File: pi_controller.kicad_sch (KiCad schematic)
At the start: 123 parts, among them J1 PWM, J10 Conn_02x08_Counter_Clockwise, J11 Conn_02x08_Counter_Clockwise, J12 Conn_02x08_Counter_Clockwise, J13 Conn_02x08_Counter_Clockwise, J14 AN1, J15 AN2, J16 AN3, J17 AN4, J18 AN5, J19 AN6, J2 I2C, J20 AN7, J21 AN8, J22 AN9, J23 AN11, J24 AN13, J25 AN15, J26 AN10, J27 AN12, J28 AN14, J29 AN16, J3 SPI_LED, J4 SPI_DISPLAY, J5 9V, J6 Conn_02x08_Counter_Clockwise, J7 Conn_02x08_Counter_Clockwise, J8 Conn_02x08_Counter_Clockwise, J9 Conn_02x08_Counter_Clockwise, Q1 AOD4184A, U1 RaspberryPi_Pico, U2 PTMUX4051DYYR, U3 PTMUX4051DYYR, U4 PTMUX4051DYYR, U5 PTMUX4051DYYR, U6 74HC595, U7 74HC595

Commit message: Initial commit
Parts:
- removed D1, D10, D11, D12, D13, D14, D15, D16, D17, D18, D19, D2, D20, D21, D22, D23, D24, D25, D26, D27, D28, D29, D3, D30, D31, D32, D33, D34, D35, D36, D37, D38, D39, D4, D40, D41, D42, D43, D44, D45, D46, D47, D48, D49, D5, D50, D51, D52, D53, D54, D55, D56, D57, D58, D59, D6, D60, D61, D62, D63, D64, D7, D8, D9: 1N4148, symbol Device:D_Small
- removed J3: SPI_LED, Connector_PinHeader_1.00mm:PinHeader_2x04_P1.00mm_Vertical, symbol Connector_Generic:Conn_02x04_Odd_Even
- removed J4: SPI_DISPLAY, Connector_PinHeader_1.00mm:PinHeader_2x04_P1.00mm_Vertical, symbol Connector_Generic:Conn_02x04_Odd_Even
- removed J5: 9V, symbol Connector_Generic:Conn_01x02
- removed R5, R7: 13k, symbol Device:R_Small
- removed U2, U3, U4, U5: PTMUX4051DYYR, SOT-23-THIN16_DYY_TEX, symbol PTMUX4051:PTMUX4051DYYR
- removed U6, U7: 74HC595, symbol 74xx:74HC595
- added C10, C12, C8, C9: 0.1uF, Capacitor_SMD:C_0201_0603Metric_Pad0.64x0.40mm_HandSolder, symbol Device:C_Small
- added C11: 100uF, Capacitor_SMD:C_0201_0603Metric_Pad0.64x0.40mm_HandSolder, symbol Device:C_Small
- added C7: 2.2uF, Capacitor_SMD:C_0201_0603Metric_Pad0.64x0.40mm_HandSolder, symbol Device:C_Small
- added D1: LED, LED_SMD:LED_0805_2012Metric_Pad1.15x1.40mm_HandSolder, symbol Device:LED
- added D10, D11, D12, D13, D14, D15, D16, D17, D18, D19, D2, D20, D21, D22, D23, D24, D25, D26, D27, D28, D29, D3, D30, D31, D32, D33, D34, D35, D36, D37, D38, D39, D4, D40, D41, D42, D43, D44, D45, D46, D47, D48, D49, D5, D50, D51, D52, D53, D54, D55, D56, D57, D58, D59, D6, D60, D61, D62, D63, D64, D65, D7, D8, D9: BAT54J, Diode_SMD:D_SOD-323F, symbol Diode:BAT54J
- added J1: DC Supply, Connector_BarrelJack:BarrelJack_Horizontal, symbol Connector:Barrel_Jack_Switch
- added J10: SPI5, Connector_PinHeader_2.54mm:PinHeader_2x03_P2.54mm_Vertical, symbol Connector_Generic:Conn_02x03_Counter_Clockwise
- added J11: SPI7, Connector_PinHeader_2.54mm:PinHeader_2x03_P2.54mm_Vertical, symbol Connector_Generic:Conn_02x03_Counter_Clockwise
- added J15: LED1, Connector_PinHeader_2.54mm:PinHeader_2x08_P2.54mm_Vertical, symbol Connector_Generic:Conn_02x08_Counter_Clockwise
- added J16: LED2, Connector_PinHeader_2.54mm:PinHeader_2x08_P2.54mm_Vertical, symbol Connector_Generic:Conn_02x08_Counter_Clockwise
- added J17: LED3, Connector_PinHeader_2.54mm:PinHeader_2x08_P2.54mm_Vertical, symbol Connector_Generic:Conn_02x08_Counter_Clockwise
- added J18: LED4, Connector_PinHeader_2.54mm:PinHeader_2x08_P2.54mm_Vertical, symbol Connector_Generic:Conn_02x08_Counter_Clockwise
- added J22: LED5, Connector_PinHeader_2.54mm:PinHeader_2x08_P2.54mm_Vertical, symbol Connector_Generic:Conn_02x08_Counter_Clockwise
- added J23: LED6, Connector_PinHeader_2.54mm:PinHeader_2x08_P2.54mm_Vertical, symbol Connector_Generic:Conn_02x08_Counter_Clockwise
- added J24: LED7, Connector_PinHeader_2.54mm:PinHeader_2x08_P2.54mm_Vertical, symbol Connector_Generic:Conn_02x08_Counter_Clockwise
- added J25: LED8, Connector_PinHeader_2.54mm:PinHeader_2x08_P2.54mm_Vertical, symbol Connector_Generic:Conn_02x08_Counter_Clockwise
- added J3: UART, Connector_PinHeader_2.54mm:PinHeader_1x04_P2.54mm_Vertical, symbol Connector_Generic:Conn_01x04
- added J5: SPI2, Connector_PinHeader_2.54mm:PinHeader_2x03_P2.54mm_Vertical, symbol Connector_Generic:Conn_02x03_Counter_Clockwise
- added J6: SPI4, Connector_PinHeader_2.54mm:PinHeader_2x03_P2.54mm_Vertical, symbol Connector_Generic:Conn_02x03_Counter_Clockwise
- added J7: SPI6, Connector_PinHeader_2.54mm:PinHeader_2x03_P2.54mm_Vertical, symbol Connector_Generic:Conn_02x03_Counter_Clockwise
- added J8: SPI8, Connector_PinHeader_2.54mm:PinHeader_2x03_P2.54mm_Vertical, symbol Connector_Generic:Conn_02x03_Counter_Clockwise
- added J9: SPI3, Connector_PinHeader_2.54mm:PinHeader_2x03_P2.54mm_Vertical, symbol Connector_Generic:Conn_02x03_Counter_Clockwise
- added L1: 3.3uH, symbol Device:L
- added R11, R12: 3.3k, Resistor_SMD:R_0603_1608Metric_Pad0.98x0.95mm_HandSolder, symbol Device:R_Small
- added TP1, TP2, TP3, TP4: TestPoint, TestPoint:TestPoint_Pad_4.0x4.0mm, symbol Connector:TestPoint
- added U1: AP62300TWU, Package_TO_SOT_SMD:TSOT-23-6, symbol Regulator_Switching:AP62300TWU
- added U3: LM4040DBZ-3, Package_TO_SOT_SMD:SOT-23, symbol Reference_Voltage:LM4040DBZ-3
- added U4, U5: 74HC138, Package_SO:SOIC-16_3.9x9.9mm_P1.27mm, symbol 74xx:74HC138
- added U6: TM1639 (TA2009B), Package_SO:SOP-24_7.5x15.4mm_P1.27mm, symbol Titan_Micro:TM1639
- added U7: CD74HC4067SM96, Package_SO:SSOP-24_5.3x8.2mm_P0.65mm, symbol 74xx:CD74HC4067SM
- C1: value 0.1uF -> 10uF; footprint (none) -> Capacitor_SMD:C_1206_3216Metric_Pad1.33x1.80mm_HandSolder; JLCPCB Part # (none) -> C13585; Package (none) -> 1206; Temperature Rating (none) -> X5R; Tolerance (none) -> 10%; Voltage Rating (none) -> 50V
- C2: value 0.1uF -> 470nF; footprint (none) -> Capacitor_SMD:C_0603_1608Metric_Pad1.08x0.95mm_HandSolder; JLCPCB Part # (none) -> C1623; Package (none) -> 0603; Temperature Rating (none) -> X7R; Tolerance (none) -> 10%; Voltage Rating (none) -> 25V
- C3: value 0.1uF -> 220nF; footprint (none) -> Capacitor_SMD:C_0603_1608Metric_Pad1.08x0.95mm_HandSolder; JLCPCB Part # (none) -> C21120; Package (none) -> 0603; Tolerance (none) -> 10%; Voltage Rating (none) -> 25V
- C4: value 0.1uF -> 100pF; footprint (none) -> Capacitor_SMD:C_0201_0603Metric_Pad0.64x0.40mm_HandSolder; JLCPCB Part # (none) -> C14663; Package (none) -> 0603; Tolerance (none) -> 10%; Voltage Rating (none) -> 50V
- C5, C6: value 0.1uF -> 22uF; footprint (none) -> Capacitor_SMD:C_1206_3216Metric_Pad1.33x1.80mm_HandSolder; JLCPCB Part # (none) -> C12891; Package (none) -> 1206; Temperature Rating (none) -> X5R; Tolerance (none) -> 10%; Voltage Rating (none) -> 25V
- J12: renamed from J6; value Conn_02x08_Counter_Clockwise -> ROW1; footprint (none) -> Connector_PinHeader_2.54mm:PinHeader_2x08_P2.54mm_Vertical
- J13: renamed from J7; value Conn_02x08_Counter_Clockwise -> ROW2; footprint (none) -> Connector_PinHeader_2.54mm:PinHeader_2x08_P2.54mm_Vertical
- J14: renamed from J8; value Conn_02x08_Counter_Clockwise -> ROW3; footprint (none) -> Connector_PinHeader_2.54mm:PinHeader_2x08_P2.54mm_Vertical
- J19: renamed from J9; value Conn_02x08_Counter_Clockwise -> ROW4; footprint (none) -> Connector_PinHeader_2.54mm:PinHeader_2x08_P2.54mm_Vertical
- J2: footprint (none) -> Connector_PinHeader_2.54mm:PinHeader_1x04_P2.54mm_Vertical
- J20: renamed from J10; value Conn_02x08_Counter_Clockwise -> ROW5; footprint (none) -> Connector_PinHeader_2.54mm:PinHeader_2x08_P2.54mm_Vertical
- J21: renamed from J11; value Conn_02x08_Counter_Clockwise -> ROW6; footprint (none) -> Connector_PinHeader_2.54mm:PinHeader_2x08_P2.54mm_Vertical
- J26: renamed from J12; value Conn_02x08_Counter_Clockwise -> ROW7; footprint (none) -> Connector_PinHeader_2.54mm:PinHeader_2x08_P2.54mm_Vertical
- J27: renamed from J13; value Conn_02x08_Counter_Clockwise -> ROW8; footprint (none) -> Connector_PinHeader_2.54mm:PinHeader_2x08_P2.54mm_Vertical
- J28: renamed from J14; footprint (none) -> Connector_PinHeader_2.54mm:PinHeader_1x03_P2.54mm_Vertical
- J29: renamed from J16; footprint (none) -> Connector_PinHeader_2.54mm:PinHeader_1x03_P2.54mm_Vertical
- J30: renamed from J18; footprint (none) -> Connector_PinHeader_2.54mm:PinHeader_1x03_P2.54mm_Vertical
- J31: renamed from J20; footprint (none) -> Connector_PinHeader_2.54mm:PinHeader_1x03_P2.54mm_Vertical
- J32: renamed from J22; footprint (none) -> Connector_PinHeader_2.54mm:PinHeader_1x03_P2.54mm_Vertical
- J33: renamed from J23; footprint (none) -> Connector_PinHeader_2.54mm:PinHeader_1x03_P2.54mm_Vertical
- J34: renamed from J24; footprint (none) -> Connector_PinHeader_2.54mm:PinHeader_1x03_P2.54mm_Vertical
- J35: renamed from J25; footprint (none) -> Connector_PinHeader_2.54mm:PinHeader_1x03_P2.54mm_Vertical
- J36: renamed from J15; footprint (none) -> Connector_PinHeader_2.54mm:PinHeader_1x03_P2.54mm_Vertical
- J37: renamed from J17; footprint (none) -> Connector_PinHeader_2.54mm:PinHeader_1x03_P2.54mm_Vertical
- J38: renamed from J19; footprint (none) -> Connector_PinHeader_2.54mm:PinHeader_1x03_P2.54mm_Vertical
- J39: renamed from J21; footprint (none) -> Connector_PinHeader_2.54mm:PinHeader_1x03_P2.54mm_Vertical
- J4: renamed from J1; footprint (none) -> Connector_PinHeader_2.54mm:PinHeader_1x03_P2.54mm_Vertical
- J40: renamed from J26; footprint (none) -> Connector_PinHeader_2.54mm:PinHeader_1x03_P2.54mm_Vertical
- J41: renamed from J27; footprint (none) -> Connector_PinHeader_2.54mm:PinHeader_1x03_P2.54mm_Vertical
- J42: renamed from J28; footprint (none) -> Connector_PinHeader_2.54mm:PinHeader_1x03_P2.54mm_Vertical
- J43: renamed from J29; footprint (none) -> Connector_PinHeader_2.54mm:PinHeader_1x03_P2.54mm_Vertical
- Q1: footprint DPAK228P994X240-4N -> Package_TO_SOT_SMD:TO-252-2; JLCPCB Part # (none) -> C99124
- R1: renamed from R9; footprint (none) -> Resistor_SMD:R_0603_1608Metric_Pad0.98x0.95mm_HandSolder; JLCPCB Part # (none) -> C4190; Package (none) -> 0603; Power (none) -> 100mW; Tolerance (none) -> 1%
- R10: value 2.2k -> 3.3k; footprint (none) -> Resistor_SMD:R_0603_1608Metric_Pad0.98x0.95mm_HandSolder; JLCPCB Part # (none) -> C22978; Package (none) -> 0603; Power (none) -> 100mW; Tolerance (none) -> 1%
- R13, R14, R15, R16: value 10k -> 3.3k; footprint (none) -> Resistor_SMD:R_0603_1608Metric_Pad0.98x0.95mm_HandSolder; JLCPCB Part # (none) -> C22978; Package (none) -> 0603; Power (none) -> 100mW; Tolerance (none) -> 1%
- R2: value 13k -> 2.2k; footprint (none) -> Resistor_SMD:R_0603_1608Metric_Pad0.98x0.95mm_HandSolder; JLCPCB Part # (none) -> C4190; Package (none) -> 0603; Power (none) -> 100mW; Tolerance (none) -> 1%
- R3: value 13k -> 10k; footprint (none) -> Resistor_SMD:R_0603_1608Metric_Pad0.98x0.95mm_HandSolder; JLCPCB Part # (none) -> C25804; Package (none) -> 0603; Power (none) -> 100mW; Tolerance (none) -> 1%
- R4: value 13k -> 33.2k; footprint (none) -> Resistor_SMD:R_0603_1608Metric_Pad0.98x0.95mm_HandSolder; JLCPCB Part # (none) -> C23003; Package (none) -> 0603; Power (none) -> 100mW; Tolerance (none) -> 1%
- R5: renamed from R11; footprint (none) -> Resistor_SMD:R_0603_1608Metric_Pad0.98x0.95mm_HandSolder; JLCPCB Part # (none) -> C22775; Package (none) -> 0603; Power (none) -> 100mW; Tolerance (none) -> 1%
- R6: value 13k -> 330; footprint (none) -> Resistor_SMD:R_0603_1608Metric_Pad0.98x0.95mm_HandSolder; JLCPCB Part # (none) -> C23137; Package (none) -> 0603; Power (none) -> 100mW; Tolerance (none) -> 1%
- R7: renamed from R12; footprint (none) -> Resistor_SMD:R_0603_1608Metric_Pad0.98x0.95mm_HandSolder; JLCPCB Part # (none) -> C25804; Package (none) -> 0603; Power (none) -> 100mW; Tolerance (none) -> 1%
- R8: value 13k -> 47R; footprint (none) -> Resistor_SMD:R_0603_1608Metric_Pad0.98x0.95mm_HandSolder; JLCPCB Part # (none) -> C23182; Package (none) -> 0603; Power (none) -> 100mW; Tolerance (none) -> 1%
- R9: renamed from R1; value 13k -> 3.3k; footprint Resistor_SMD:R_0805_2012Metric -> Resistor_SMD:R_0603_1608Metric_Pad0.98x0.95mm_HandSolder; JLCPCB Part # (none) -> C22978; Package (none) -> 0603; Power (none) -> 100mW; Tolerance (none) -> 1%
- renumbered U1 to U2
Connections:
- net ADC0_MUX_CS is gone; now on net ROW6: U2.10 (GPIO7)
- net ADC1 is gone; now on net CS_LED: U2.32 (GPIO27_ADC1)
- net ROW_INPUT is gone; now on net ROW1: U2.1 (GPIO0)
- net ROW_MUX_A is gone; now on net ROW2: U2.2 (GPIO1)
- net ROW_MUX_B is gone; now on net ROW3: U2.4 (GPIO2)
- net ROW_MUX_C is gone; now on net ROW4: U2.5 (GPIO3)
- net ROW_MUX_CS is gone; now on net ROW5: U2.9 (GPIO6)
- net STEP_EN is gone; now on net ROW7: U2.19 (GPIO14)
- net STEP_RST is gone; now on net ROW8: U2.20 (GPIO15)
- net +3V3: now also C4.2, C5.2, C6.2, R10.1, R2.2, R4.2, R6.2, C10.1, C11.1, C12.1, C8.1, C9.1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; no longer C1.1, C2.1, C3.1, C4.1, C5.1, C6.1, J28.1 (Pin_1), J29.1 (Pin_1), J30.1 (Pin_1), J31.1 (Pin_1), J32.1 (Pin_1), J33.1 (Pin_1)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
- net +9V: now also C1.2, J1.1, U1.3 (IN)
- net ADC0: now also U7.1 (COM)
- net AN1: now also U7.9 (I0)
- net AN10: now also U7.22 (I9)
- net AN11: now also U7.21 (I10)
- net AN12: now also U7.20 (I11)
- net AN13: now also U7.19 (I12)
- net AN14: now also U7.18 (I13)
- net AN15: now also U7.17 (I14)
- net AN16: now also U7.16 (I15)
- net AN2: now also U7.8 (I1)
- net AN3: now also U7.7 (I2)
- net AN4: now also U7.6 (I3)
- net AN5: now also U7.5 (I4)
- net AN6: now also U7.4 (I5)
- net AN7: now also U7.3 (I6)
- net AN8: now also U7.2 (I7)
- net AN9: now also U7.23 (I8)
- net COL1: now also D2.1 (K), D26.1 (K), D27.1 (K), D28.1 (K), D3.1 (K), D4.1 (K), D50.1 (K), D51.1 (K), U4.15 (~{Y0})
- net COL2: now also D29.1 (K), D30.1 (K), D31.1 (K), D5.1 (K), D52.1 (K), D53.1 (K), D6.1 (K), D7.1 (K), U4.14 (~{Y1})
- net COL3: now also D10.1 (K), D32.1 (K), D33.1 (K), D34.1 (K), D54.1 (K), D55.1 (K), D8.1 (K), D9.1 (K), U4.13 (~{Y2})
- net COL4: now also D11.1 (K), D12.1 (K), D13.1 (K), D35.1 (K), D36.1 (K), D37.1 (K), D56.1 (K), D57.1 (K), U4.12 (~{Y3})
- net COL5: now also D14.1 (K), D15.1 (K), D16.1 (K), D38.1 (K), D39.1 (K), D40.1 (K), D58.1 (K), D59.1 (K), U4.11 (~{Y4})
- net COL6: now also D17.1 (K), D18.1 (K), D19.1 (K), D41.1 (K), D42.1 (K), D43.1 (K), D60.1 (K), D61.1 (K), U4.10 (~{Y5})
- net COL7: now also D20.1 (K), D21.1 (K), D22.1 (K), D44.1 (K), D45.1 (K), D46.1 (K), D62.1 (K), D63.1 (K), U4.9 (~{Y6})
- net COL8: now also D23.1 (K), D24.1 (K), D25.1 (K), D47.1 (K), D48.1 (K), D49.1 (K), D64.1 (K), D65.1 (K), U4.7 (~{Y7})
- net COL_MUX_A: now also U4.1 (A0), U5.1 (A0)
- net COL_MUX_B: now also U4.2 (A1), U5.2 (A1)
- net COL_MUX_C: now also U4.3 (A2), U5.3 (A2)
- net CS_LED: now also U5.6 (E2); no longer U2.22 (GPIO17)
- net GND: now also C1.1, C2.1, C5.1, C6.1, R3.1, C10.2, C11.2, C12.2, C7.2, C8.2, C9.2, D1.1 (K)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; no longer C1.2, C2.2, C3.2, C4.2, C5.2, C6.2
- net MISO: now also J10.5 (Pin_5), J11.5 (Pin_5), J5.5 (Pin_5), J6.5 (Pin_5), J7.5 (Pin_5), J8.5 (Pin_5), J9.5 (Pin_5)
- net MOSI: now also J10.1 (Pin_1), J11.1 (Pin_1), J5.1 (Pin_1), J6.1 (Pin_1), J7.1 (Pin_1), J8.1 (Pin_1), J9.1 (Pin_1), U6.6 (DIO)
- net ROW2: now also R10.2; no longer R2.2
- net ROW3: now also R11.2; no longer R3.2
- net ROW4: now also R12.2; no longer R4.2
- net ROW5: now also R13.2
- net ROW6: now also R14.2; no longer R6.2
- net ROW7: now also R15.2
- net ROW8: now also R16.2; no longer R8.2
- net +3.3VA renamed VDDA
- net ADC1_MUX_CS renamed ADC_MUX_B
- removed net CLR: R13.2, R16.2
- net COL_MUX_CS renamed ADC_MUX_D
- net CS_DISPLAY renamed ADC_MUX_A
- removed net OE_LED: R14.2, R15.2
- net STEP_CLK renamed UART0_RX
- net STEP_DIR renamed UART0_TX
- net STEP_SLEEP renamed ADC_MUX_C
- new net: C4.1, R3.2, R4.1, U1.4 (FB)
- new net: C3.1, U1.6 (BST)
- new net: C3.2, L1.1, U1.2 (SW)
- new net: C2.2, U1.5 (EN)
- new net: D1.2 (A), R6.1, TP2.1
- new net CS1: U5.15 (~{Y0}), U6.8 (~{STB})
- new net CS2: J5.3 (Pin_3), U5.14 (~{Y1})
- new net CS3: J9.3 (Pin_3), U5.13 (~{Y2})
- new net CS4: J6.3 (Pin_3), U5.12 (~{Y3})
- new net CS5: J10.3 (Pin_3), U5.11 (~{Y4})
- new net CS6: J7.3 (Pin_3), U5.10 (~{Y5})
- new net CS7: J11.3 (Pin_3), U5.9 (~{Y6})
- new net CS8: J8.3 (Pin_3), U5.7 (~{Y7})
- new net CS_KEY: U2.22 (GPIO17), U4.6 (E2)
- new net GRID1: J15.1 (Pin_1), J16.1 (Pin_1), J17.1 (Pin_1), J18.1 (Pin_1), J22.1 (Pin_1), J23.1 (Pin_1), J24.1 (Pin_1), J25.1 (Pin_1), U6.5 (GRID1)
- new net GRID2: J15.2 (Pin_2), J16.2 (Pin_2), J17.2 (Pin_2), J18.2 (Pin_2), J22.2 (Pin_2), J23.2 (Pin_2), J24.2 (Pin_2), J25.2 (Pin_2), U6.4 (GRID2)
- new net GRID3: J15.3 (Pin_3), J16.3 (Pin_3), J17.3 (Pin_3), J18.3 (Pin_3), J22.3 (Pin_3), J23.3 (Pin_3), J24.3 (Pin_3), J25.3 (Pin_3), U6.2 (GRID3)
- new net GRID4: J15.4 (Pin_4), J16.4 (Pin_4), J17.4 (Pin_4), J18.4 (Pin_4), J22.4 (Pin_4), J23.4 (Pin_4), J24.4 (Pin_4), J25.4 (Pin_4), U6.1 (GRID4)
- new net GRID5: J15.5 (Pin_5), J16.5 (Pin_5), J17.5 (Pin_5), J18.5 (Pin_5), J22.5 (Pin_5), J23.5 (Pin_5), J24.5 (Pin_5), J25.5 (Pin_5), U6.24 (GRID5)
- new net GRID6: J15.6 (Pin_6), J16.6 (Pin_6), J17.6 (Pin_6), J18.6 (Pin_6), J22.6 (Pin_6), J23.6 (Pin_6), J24.6 (Pin_6), J25.6 (Pin_6), U6.23 (GRID6)
- new net GRID7: J15.7 (Pin_7), J16.7 (Pin_7), J17.7 (Pin_7), J18.7 (Pin_7), J22.7 (Pin_7), J23.7 (Pin_7), J24.7 (Pin_7), J25.7 (Pin_7), U6.21 (GRID7)
- new net GRID8: J15.8 (Pin_8), J16.8 (Pin_8), J17.8 (Pin_8), J18.8 (Pin_8), J22.8 (Pin_8), J23.8 (Pin_8), J24.8 (Pin_8), J25.8 (Pin_8), U6.20 (GRID8)
- new net SEG1: J15.10 (Pin_10), J15.11 (Pin_11), J15.12 (Pin_12), J15.13 (Pin_13), J15.14 (Pin_14), J15.15 (Pin_15), J15.16 (Pin_16), J15.9 (Pin_9), U6.12 (SEG1/KS1)
- new net SEG10: J23.10 (Pin_10), J23.11 (Pin_11), J23.12 (Pin_12), J23.13 (Pin_13), J23.14 (Pin_14), J23.15 (Pin_15), J23.16 (Pin_16), J23.9 (Pin_9), U6.17 (SEG10)
- new net SEG11: J24.10 (Pin_10), J24.11 (Pin_11), J24.12 (Pin_12), J24.13 (Pin_13), J24.14 (Pin_14), J24.15 (Pin_15), J24.16 (Pin_16), J24.9 (Pin_9), U6.18 (SEG11)
- new net SEG12: J25.10 (Pin_10), J25.11 (Pin_11), J25.12 (Pin_12), J25.13 (Pin_13), J25.14 (Pin_14), J25.15 (Pin_15), J25.16 (Pin_16), J25.9 (Pin_9), U6.19 (SEG12)
- new net SEG2: J16.10 (Pin_10), J16.11 (Pin_11), J16.12 (Pin_12), J16.13 (Pin_13), J16.14 (Pin_14), J16.15 (Pin_15), J16.16 (Pin_16), J16.9 (Pin_9), U6.13 (SEG2/KS2)
- new net SEG3: J17.10 (Pin_10), J17.11 (Pin_11), J17.12 (Pin_12), J17.13 (Pin_13), J17.14 (Pin_14), J17.15 (Pin_15), J17.16 (Pin_16), J17.9 (Pin_9), U6.14 (SEG3/KS3)
- new net SEG4: J18.10 (Pin_10), J18.11 (Pin_11), J18.12 (Pin_12), J18.13 (Pin_13), J18.14 (Pin_14), J18.15 (Pin_15), J18.16 (Pin_16), J18.9 (Pin_9), U6.15 (SEG4/KS4)
- new net SEG9: J22.10 (Pin_10), J22.11 (Pin_11), J22.12 (Pin_12), J22.13 (Pin_13), J22.14 (Pin_14), J22.15 (Pin_15), J22.16 (Pin_16), J22.9 (Pin_9), U6.16 (SEG9)
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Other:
- note added: "I2C Output"
- note added: "Power Supply"
- note added: "UART Output"
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
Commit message: Update layout and rules
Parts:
- removed J10: SPI5, Connector_PinHeader_2.54mm:PinHeader_2x03_P2.54mm_Vertical, symbol Connector_Generic:Conn_02x03_Counter_Clockwise
- removed J11: SPI7, Connector_PinHeader_2.54mm:PinHeader_2x03_P2.54mm_Vertical, symbol Connector_Generic:Conn_02x03_Counter_Clockwise
- removed J12: ROW1, Connector_PinHeader_2.54mm:PinHeader_2x08_P2.54mm_Vertical, symbol Connector_Generic:Conn_02x08_Counter_Clockwise
- removed J13: ROW2, Connector_PinHeader_2.54mm:PinHeader_2x08_P2.54mm_Vertical, symbol Connector_Generic:Conn_02x08_Counter_Clockwise
- removed J14: ROW3, Connector_PinHeader_2.54mm:PinHeader_2x08_P2.54mm_Vertical, symbol Connector_Generic:Conn_02x08_Counter_Clockwise
- removed J15: LED1, Connector_PinHeader_2.54mm:PinHeader_2x08_P2.54mm_Vertical, symbol Connector_Generic:Conn_02x08_Counter_Clockwise
- removed J16: LED2, Connector_PinHeader_2.54mm:PinHeader_2x08_P2.54mm_Vertical, symbol Connector_Generic:Conn_02x08_Counter_Clockwise
- removed J17: LED3, Connector_PinHeader_2.54mm:PinHeader_2x08_P2.54mm_Vertical, symbol Connector_Generic:Conn_02x08_Counter_Clockwise
- removed J18: LED4, Connector_PinHeader_2.54mm:PinHeader_2x08_P2.54mm_Vertical, symbol Connector_Generic:Conn_02x08_Counter_Clockwise
- removed J19: ROW4, Connector_PinHeader_2.54mm:PinHeader_2x08_P2.54mm_Vertical, symbol Connector_Generic:Conn_02x08_Counter_Clockwise
- removed J20: ROW5, Connector_PinHeader_2.54mm:PinHeader_2x08_P2.54mm_Vertical, symbol Connector_Generic:Conn_02x08_Counter_Clockwise
- removed J21: ROW6, Connector_PinHeader_2.54mm:PinHeader_2x08_P2.54mm_Vertical, symbol Connector_Generic:Conn_02x08_Counter_Clockwise
- removed J22: LED5, Connector_PinHeader_2.54mm:PinHeader_2x08_P2.54mm_Vertical, symbol Connector_Generic:Conn_02x08_Counter_Clockwise
- removed J23: LED6, Connector_PinHeader_2.54mm:PinHeader_2x08_P2.54mm_Vertical, symbol Connector_Generic:Conn_02x08_Counter_Clockwise
- removed J24: LED7, Connector_PinHeader_2.54mm:PinHeader_2x08_P2.54mm_Vertical, symbol Connector_Generic:Conn_02x08_Counter_Clockwise
- removed J25: LED8, Connector_PinHeader_2.54mm:PinHeader_2x08_P2.54mm_Vertical, symbol Connector_Generic:Conn_02x08_Counter_Clockwise
- removed J26: ROW7, Connector_PinHeader_2.54mm:PinHeader_2x08_P2.54mm_Vertical, symbol Connector_Generic:Conn_02x08_Counter_Clockwise
- removed J27: ROW8, Connector_PinHeader_2.54mm:PinHeader_2x08_P2.54mm_Vertical, symbol Connector_Generic:Conn_02x08_Counter_Clockwise
- removed J5: SPI2, Connector_PinHeader_2.54mm:PinHeader_2x03_P2.54mm_Vertical, symbol Connector_Generic:Conn_02x03_Counter_Clockwise
- removed J6: SPI4, Connector_PinHeader_2.54mm:PinHeader_2x03_P2.54mm_Vertical, symbol Connector_Generic:Conn_02x03_Counter_Clockwise
- removed J7: SPI6, Connector_PinHeader_2.54mm:PinHeader_2x03_P2.54mm_Vertical, symbol Connector_Generic:Conn_02x03_Counter_Clockwise
- removed J8: SPI8, Connector_PinHeader_2.54mm:PinHeader_2x03_P2.54mm_Vertical, symbol Connector_Generic:Conn_02x03_Counter_Clockwise
- removed J9: SPI3, Connector_PinHeader_2.54mm:PinHeader_2x03_P2.54mm_Vertical, symbol Connector_Generic:Conn_02x03_Counter_Clockwise
- added J10: CS5, Connector_PinHeader_2.54mm:PinHeader_2x03_P2.54mm_Vertical, symbol Connector_Generic:Conn_02x03_Odd_Even
- added J11: CS7, Connector_PinHeader_2.54mm:PinHeader_2x03_P2.54mm_Vertical, symbol Connector_Generic:Conn_02x03_Odd_Even
- added J12: ROW1, Connector_PinHeader_2.54mm:PinHeader_2x08_P2.54mm_Vertical, symbol Connector_Generic:Conn_02x08_Odd_Even
- added J13: ROW2, Connector_PinHeader_2.54mm:PinHeader_2x08_P2.54mm_Vertical, symbol Connector_Generic:Conn_02x08_Odd_Even
- added J14: ROW3, Connector_PinHeader_2.54mm:PinHeader_2x08_P2.54mm_Vertical, symbol Connector_Generic:Conn_02x08_Odd_Even
- added J15: LED1, Connector_PinHeader_2.54mm:PinHeader_2x08_P2.54mm_Vertical, symbol Connector_Generic:Conn_02x08_Odd_Even
- added J16: LED2, Connector_PinHeader_2.54mm:PinHeader_2x08_P2.54mm_Vertical, symbol Connector_Generic:Conn_02x08_Odd_Even
- added J17: LED3, Connector_PinHeader_2.54mm:PinHeader_2x08_P2.54mm_Vertical, symbol Connector_Generic:Conn_02x08_Odd_Even
- added J18: LED4, Connector_PinHeader_2.54mm:PinHeader_2x08_P2.54mm_Vertical, symbol Connector_Generic:Conn_02x08_Odd_Even
- added J19: ROW4, Connector_PinHeader_2.54mm:PinHeader_2x08_P2.54mm_Vertical, symbol Connector_Generic:Conn_02x08_Odd_Even
- added J20: ROW5, Connector_PinHeader_2.54mm:PinHeader_2x08_P2.54mm_Vertical, symbol Connector_Generic:Conn_02x08_Odd_Even
- added J21: ROW6, Connector_PinHeader_2.54mm:PinHeader_2x08_P2.54mm_Vertical, symbol Connector_Generic:Conn_02x08_Odd_Even
- added J22: LED5, Connector_PinHeader_2.54mm:PinHeader_2x08_P2.54mm_Vertical, symbol Connector_Generic:Conn_02x08_Odd_Even
- added J23: LED6, Connector_PinHeader_2.54mm:PinHeader_2x08_P2.54mm_Vertical, symbol Connector_Generic:Conn_02x08_Odd_Even
- added J24: LED7, Connector_PinHeader_2.54mm:PinHeader_2x08_P2.54mm_Vertical, symbol Connector_Generic:Conn_02x08_Odd_Even
- added J25: LED8, Connector_PinHeader_2.54mm:PinHeader_2x08_P2.54mm_Vertical, symbol Connector_Generic:Conn_02x08_Odd_Even
- added J26: ROW7, Connector_PinHeader_2.54mm:PinHeader_2x08_P2.54mm_Vertical, symbol Connector_Generic:Conn_02x08_Odd_Even
- added J27: ROW8, Connector_PinHeader_2.54mm:PinHeader_2x08_P2.54mm_Vertical, symbol Connector_Generic:Conn_02x08_Odd_Even
- added J5: CS2, Connector_PinHeader_2.54mm:PinHeader_2x03_P2.54mm_Vertical, symbol Connector_Generic:Conn_02x03_Odd_Even
- added J6: CS4, Connector_PinHeader_2.54mm:PinHeader_2x03_P2.54mm_Vertical, symbol Connector_Generic:Conn_02x03_Odd_Even
- added J7: CS6, Connector_PinHeader_2.54mm:PinHeader_2x03_P2.54mm_Vertical, symbol Connector_Generic:Conn_02x03_Odd_Even
- added J8: CS8, Connector_PinHeader_2.54mm:PinHeader_2x03_P2.54mm_Vertical, symbol Connector_Generic:Conn_02x03_Odd_Even
- added J9: CS3, Connector_PinHeader_2.54mm:PinHeader_2x03_P2.54mm_Vertical, symbol Connector_Generic:Conn_02x03_Odd_Even
- L1: footprint (none) -> Inductor_SMD:L_Sunlord_MWSA0604S
- renumbered TP3 to TP1, TP1 to TP2, TP2 to TP3
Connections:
- net +3V3: now also J10.2 (Pin_2), J11.2 (Pin_2), J5.2 (Pin_2), J6.2 (Pin_2), J7.2 (Pin_2), J8.2 (Pin_2), J9.2 (Pin_2)
- net CS2: now also J5.5 (Pin_5)
- net CS3: now also J9.5 (Pin_5)
- net CS4: now also J6.5 (Pin_5)
- net CS5: now also J10.5 (Pin_5)
- net CS6: now also J7.5 (Pin_5)
- net CS7: now also J11.5 (Pin_5)
- net CS8: now also J8.5 (Pin_5)
- net GND: now also J10.6 (Pin_6), J11.6 (Pin_6), J5.6 (Pin_6), J6.6 (Pin_6), J7.6 (Pin_6), J8.6 (Pin_6), J9.6 (Pin_6)
- net GRID1: now also J15.16 (Pin_16), J16.16 (Pin_16), J17.16 (Pin_16), J18.16 (Pin_16), J22.16 (Pin_16), J23.16 (Pin_16), J24.16 (Pin_16), J25.16 (Pin_16)
- net GRID2: now also J15.14 (Pin_14), J16.14 (Pin_14), J17.14 (Pin_14), J18.14 (Pin_14), J22.14 (Pin_14), J23.14 (Pin_14), J24.14 (Pin_14), J25.14 (Pin_14)
- net GRID3: now also J15.12 (Pin_12), J16.12 (Pin_12), J17.12 (Pin_12), J18.12 (Pin_12), J22.12 (Pin_12), J23.12 (Pin_12), J24.12 (Pin_12), J25.12 (Pin_12)
- net GRID4: now also J15.10 (Pin_10), J16.10 (Pin_10), J17.10 (Pin_10), J18.10 (Pin_10), J22.10 (Pin_10), J23.10 (Pin_10), J24.10 (Pin_10), J25.10 (Pin_10)
- net GRID5: now also J15.8 (Pin_8), J16.8 (Pin_8), J17.8 (Pin_8), J18.8 (Pin_8), J22.8 (Pin_8), J23.8 (Pin_8), J24.8 (Pin_8), J25.8 (Pin_8)
- net GRID6: now also J15.6 (Pin_6), J16.6 (Pin_6), J17.6 (Pin_6), J18.6 (Pin_6), J22.6 (Pin_6), J23.6 (Pin_6), J24.6 (Pin_6), J25.6 (Pin_6)
- net GRID7: now also J15.4 (Pin_4), J16.4 (Pin_4), J17.4 (Pin_4), J18.4 (Pin_4), J22.4 (Pin_4), J23.4 (Pin_4), J24.4 (Pin_4), J25.4 (Pin_4)
- net GRID8: now also J15.2 (Pin_2), J16.2 (Pin_2), J17.2 (Pin_2), J18.2 (Pin_2), J22.2 (Pin_2), J23.2 (Pin_2), J24.2 (Pin_2), J25.2 (Pin_2)
- net MISO: now also J10.4 (Pin_4), J11.4 (Pin_4), J5.4 (Pin_4), J6.4 (Pin_4), J7.4 (Pin_4), J8.4 (Pin_4), J9.4 (Pin_4)
- net MOSI: now also J10.1 (Pin_1), J11.1 (Pin_1), J5.1 (Pin_1), J6.1 (Pin_1), J7.1 (Pin_1), J8.1 (Pin_1), J9.1 (Pin_1)
- net ROW1: now also J12.10 (Pin_10), J12.12 (Pin_12), J12.14 (Pin_14), J12.16 (Pin_16), J12.2 (Pin_2), J12.4 (Pin_4), J12.6 (Pin_6), J12.8 (Pin_8)
- net ROW2: now also J13.10 (Pin_10), J13.12 (Pin_12), J13.14 (Pin_14), J13.16 (Pin_16), J13.2 (Pin_2), J13.4 (Pin_4), J13.6 (Pin_6), J13.8 (Pin_8)
- net ROW3: now also J14.10 (Pin_10), J14.12 (Pin_12), J14.14 (Pin_14), J14.16 (Pin_16), J14.2 (Pin_2), J14.4 (Pin_4), J14.6 (Pin_6), J14.8 (Pin_8)
- net ROW4: now also J19.10 (Pin_10), J19.12 (Pin_12), J19.14 (Pin_14), J19.16 (Pin_16), J19.2 (Pin_2), J19.4 (Pin_4), J19.6 (Pin_6), J19.8 (Pin_8)
- net ROW5: now also J20.10 (Pin_10), J20.12 (Pin_12), J20.14 (Pin_14), J20.16 (Pin_16), J20.2 (Pin_2), J20.4 (Pin_4), J20.6 (Pin_6), J20.8 (Pin_8)
- net ROW6: now also J21.10 (Pin_10), J21.12 (Pin_12), J21.14 (Pin_14), J21.16 (Pin_16), J21.2 (Pin_2), J21.4 (Pin_4), J21.6 (Pin_6), J21.8 (Pin_8)
- net ROW7: now also J26.10 (Pin_10), J26.12 (Pin_12), J26.14 (Pin_14), J26.16 (Pin_16), J26.2 (Pin_2), J26.4 (Pin_4), J26.6 (Pin_6), J26.8 (Pin_8)
- net ROW8: now also J27.10 (Pin_10), J27.12 (Pin_12), J27.14 (Pin_14), J27.16 (Pin_16), J27.2 (Pin_2), J27.4 (Pin_4), J27.6 (Pin_6), J27.8 (Pin_8)
- net SCLK: now also J10.3 (Pin_3), J11.3 (Pin_3), J5.3 (Pin_3), J6.3 (Pin_3), J7.3 (Pin_3), J8.3 (Pin_3), J9.3 (Pin_3)
- net SEG1: now also J15.1 (Pin_1), J15.11 (Pin_11), J15.13 (Pin_13), J15.15 (Pin_15), J15.3 (Pin_3), J15.5 (Pin_5), J15.7 (Pin_7), J15.9 (Pin_9)
- net SEG10: now also J23.1 (Pin_1), J23.11 (Pin_11), J23.13 (Pin_13), J23.15 (Pin_15), J23.3 (Pin_3), J23.5 (Pin_5), J23.7 (Pin_7), J23.9 (Pin_9)
- net SEG11: now also J24.1 (Pin_1), J24.11 (Pin_11), J24.13 (Pin_13), J24.15 (Pin_15), J24.3 (Pin_3), J24.5 (Pin_5), J24.7 (Pin_7), J24.9 (Pin_9)
- net SEG12: now also J25.1 (Pin_1), J25.11 (Pin_11), J25.13 (Pin_13), J25.15 (Pin_15), J25.3 (Pin_3), J25.5 (Pin_5), J25.7 (Pin_7), J25.9 (Pin_9)
- net SEG2: now also J16.1 (Pin_1), J16.11 (Pin_11), J16.13 (Pin_13), J16.15 (Pin_15), J16.3 (Pin_3), J16.5 (Pin_5), J16.7 (Pin_7), J16.9 (Pin_9)
- net SEG3: now also J17.1 (Pin_1), J17.11 (Pin_11), J17.13 (Pin_13), J17.15 (Pin_15), J17.3 (Pin_3), J17.5 (Pin_5), J17.7 (Pin_7), J17.9 (Pin_9)
- net SEG4: now also J18.1 (Pin_1), J18.11 (Pin_11), J18.13 (Pin_13), J18.15 (Pin_15), J18.3 (Pin_3), J18.5 (Pin_5), J18.7 (Pin_7), J18.9 (Pin_9)
- net SEG9: now also J22.1 (Pin_1), J22.11 (Pin_11), J22.13 (Pin_13), J22.15 (Pin_15), J22.3 (Pin_3), J22.5 (Pin_5), J22.7 (Pin_7), J22.9 (Pin_9)
- net at D51.2 (A): now also J27.1 (Pin_1)
- net at D5.2 (A): now also J12.3 (Pin_3)
- net at D64.2 (A): now also J26.15 (Pin_15)
- net at D46.2 (A): now also J21.13 (Pin_13)
- net at D27.2 (A): now also J20.1 (Pin_1)
- net at D30.2 (A): now also J20.3 (Pin_3)
- net at D33.2 (A): now also J20.5 (Pin_5)
- net at D36.2 (A): now also J20.7 (Pin_7)
- net at D39.2 (A): now also J20.9 (Pin_9)
- net at D42.2 (A): now also J20.11 (Pin_11)
- net at D45.2 (A): now also J20.13 (Pin_13)
- net at D48.2 (A): now also J20.15 (Pin_15)
- net at D47.2 (A): now also J19.15 (Pin_15)
- net at D11.2 (A): now also J12.7 (Pin_7)
- net at D50.2 (A): now also J26.1 (Pin_1)
- net at D52.2 (A): now also J26.3 (Pin_3)
- net at D54.2 (A): now also J26.5 (Pin_5)
- net at D56.2 (A): now also J26.7 (Pin_7)
- net at D58.2 (A): now also J26.9 (Pin_9)
- net at D60.2 (A): now also J26.11 (Pin_11)
- net at D62.2 (A): now also J26.13 (Pin_13)
- net at D10.2 (A): now also J14.5 (Pin_5)
- net at D57.2 (A): now also J27.7 (Pin_7)
- net at D28.2 (A): now also J21.1 (Pin_1)
- net at D31.2 (A): now also J21.3 (Pin_3)
- net at D34.2 (A): now also J21.5 (Pin_5)
- net at D37.2 (A): now also J21.7 (Pin_7)
- net at D40.2 (A): now also J21.9 (Pin_9)
- net at D43.2 (A): now also J21.11 (Pin_11)
- net at D49.2 (A): now also J21.15 (Pin_15)
- net at D41.2 (A): now also J19.11 (Pin_11)
- net at D18.2 (A): now also J13.11 (Pin_11)
- net at D19.2 (A): now also J14.11 (Pin_11)
- net at D2.2 (A): now also J12.1 (Pin_1)
- net at D6.2 (A): now also J13.3 (Pin_3)
- net at D3.2 (A): now also J13.1 (Pin_1)
- net at D9.2 (A): now also J13.5 (Pin_5)
- net at D12.2 (A): now also J13.7 (Pin_7)
- net at D15.2 (A): now also J13.9 (Pin_9)
- net at D21.2 (A): now also J13.13 (Pin_13)
- net at D24.2 (A): now also J13.15 (Pin_15)
- net at D32.2 (A): now also J19.5 (Pin_5)
- net at D65.2 (A): now also J27.15 (Pin_15)
- net at D59.2 (A): now also J27.9 (Pin_9)
- net at D26.2 (A): now also J19.1 (Pin_1)
- net at D8.2 (A): now also J12.5 (Pin_5)
- net at D14.2 (A): now also J12.9 (Pin_9)
- net at D17.2 (A): now also J12.11 (Pin_11)
- net at D20.2 (A): now also J12.13 (Pin_13)
- net at D23.2 (A): now also J12.15 (Pin_15)
- net at D29.2 (A): now also J19.3 (Pin_3)
- net at D35.2 (A): now also J19.7 (Pin_7)
- net at D38.2 (A): now also J19.9 (Pin_9)
- net at D44.2 (A): now also J19.13 (Pin_13)
- net at J4.2 (Pin_2): now also Q1.2; no longer Q1.4
- net at D13.2 (A): now also J14.7 (Pin_7)
- net at D61.2 (A): now also J27.11 (Pin_11)
- net at D53.2 (A): now also J27.3 (Pin_3)
- net at D55.2 (A): now also J27.5 (Pin_5)
- net at D63.2 (A): now also J27.13 (Pin_13)
- net at D4.2 (A): now also J14.1 (Pin_1)
- net at D7.2 (A): now also J14.3 (Pin_3)
- net at D16.2 (A): now also J14.9 (Pin_9)
- net at D22.2 (A): now also J14.13 (Pin_13)
- net at D25.2 (A): now also J14.15 (Pin_15)

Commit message: Update routing
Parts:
- added H1, H2, H3, H4: MountingHole_Pad, MountingHole:MountingHole_2.2mm_M2_ISO14580_Pad_TopBottom, symbol Mechanical:MountingHole_Pad
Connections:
- net GND: now also H1.1, H2.1, H3.1, H4.1

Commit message: Adjusting DRC checks
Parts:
- TP1, TP2, TP3, TP4: footprint TestPoint:TestPoint_Pad_4.0x4.0mm -> TestPoint:TestPoint_Pad_D4.0mm
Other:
- company: Carlos Eduardo de Almeida Mazzei -> Carlos Mazzei
- title: Raspberry Pi Pico Controller -> PiMax - Raspberry Pi Pico Breakout Board
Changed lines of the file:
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@@
 	(paper "A2")
 	(title_block
-		(title "Raspberry Pi Pico Controller")
-		(date "2023-08-03")
+		(title "PiMax - Raspberry Pi Pico Breakout Board")
+		(date "2025-03-08")
 		(rev "1")
-		(company "Carlos Eduardo de Almeida Mazzei")
+		(company "Carlos Mazzei")
 		(comment 1 "Controller board for common inputs and outputs")
 	)
@@
 			)
 		)
-		(property "Footprint" "TestPoint:TestPoint_Pad_4.0x4.0mm"
+		(property "Footprint" "TestPoint:TestPoint_Pad_D4.0mm"
 			(at 138.43 74.93 0)
 			(effects
@@
 			)
 		)
-		(property "Footprint" "TestPoint:TestPoint_Pad_4.0x4.0mm"
+		(property "Footprint" "TestPoint:TestPoint_Pad_D4.0mm"
 			(at 180.34 270.51 0)
 			(effects
@@
 			)
 		)
-		(property "Footprint" "TestPoint:TestPoint_Pad_4.0x4.0mm"
+		(property "Footprint" "TestPoint:TestPoint_Pad_D4.0mm"
 			(at 95.25 85.09 0)
 			(effects
@@
 			)
 		)
-		(property "Footprint" "TestPoint:TestPoint_Pad_4.0x4.0mm"
+		(property "Footprint" "TestPoint:TestPoint_Pad_D4.0mm"
 			(at 168.91 83.82 0)
 			(effects

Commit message: Refining layout
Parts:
- renumbered J28 to AN1, J40 to AN10, J33 to AN11, J41 to AN12, J34 to AN13, J42 to AN14, J35 to AN15, J43 to AN16, J36 to AN2, J29 to AN3, J37 to AN4, J30 to AN5, J38 to AN6, J31 to AN7, J39 to AN8, J32 to AN9, C12 to C1, C11 to C10, C10 to C11, C8 to C12, C5 to C2, C6 to C3, C1 to C4, C2 to C5, C3 to C6, C4 to C7, C7 to C8, D12 to D10, D5 to D12, D6 to D13, D9 to D14, D21 to D15, D47 to D16, D45 to D17, D44 to D18, D48 to D19, D8 to D2, D42 to D20, D41 to D21, D39 to D22, D38 to D23, D36 to D24, D35 to D25, D19 to D26, D33 to D27, D32 to D28, D22 to D29, D23 to D3, D29 to D31, D13 to D32, D10 to D33, D16 to D34, D25 to D35, D7 to D36, D62 to D37, D56 to D38, D58 to D39, D24 to D4, D31 to D40, D34 to D41, D37 to D42, D40 to D43, D43 to D44, D46 to D45, D49 to D46, D64 to D47, D52 to D48, D60 to D49, D20 to D5, D54 to D50, D59 to D51, D63 to D52, D61 to D53, D65 to D54, D57 to D55, D53 to D56, D55 to D57, D2 to D58, D3 to D59, D18 to D6, D4 to D60, D27 to D61, D26 to D62, D50 to D63, D28 to D64, D51 to D65, D17 to D7, D15 to D8, D14 to D9, H2 to H1, H3 to H2, H4 to H3, H1 to H4, J4 to J1, J5 to J17, J6 to J18, J7 to J19, J1 to J2, J8 to J20, J9 to J21, J10 to J22, J11 to J23, J23 to J26, J22 to J27, J24 to J28, J25 to J29, J2 to J30, J3 to J31, J17 to J32, J15 to J33, J16 to J34, J18 to J35, J12 to J36, J13 to J37, J14 to J38, J20 to J39, J19 to J40, J21 to J41, J26 to J42, J27 to J43, R3 to R1, R11 to R10, R10 to R11, R15 to R14, R16 to R15, R14 to R16, R4 to R2, R5 to R3, R6 to R4, R7 to R5, R8 to R6, R1 to R7, R2 to R8, TP4 to TP2, TP2 to TP4, U7 to U2, U2 to U4, U4 to U7

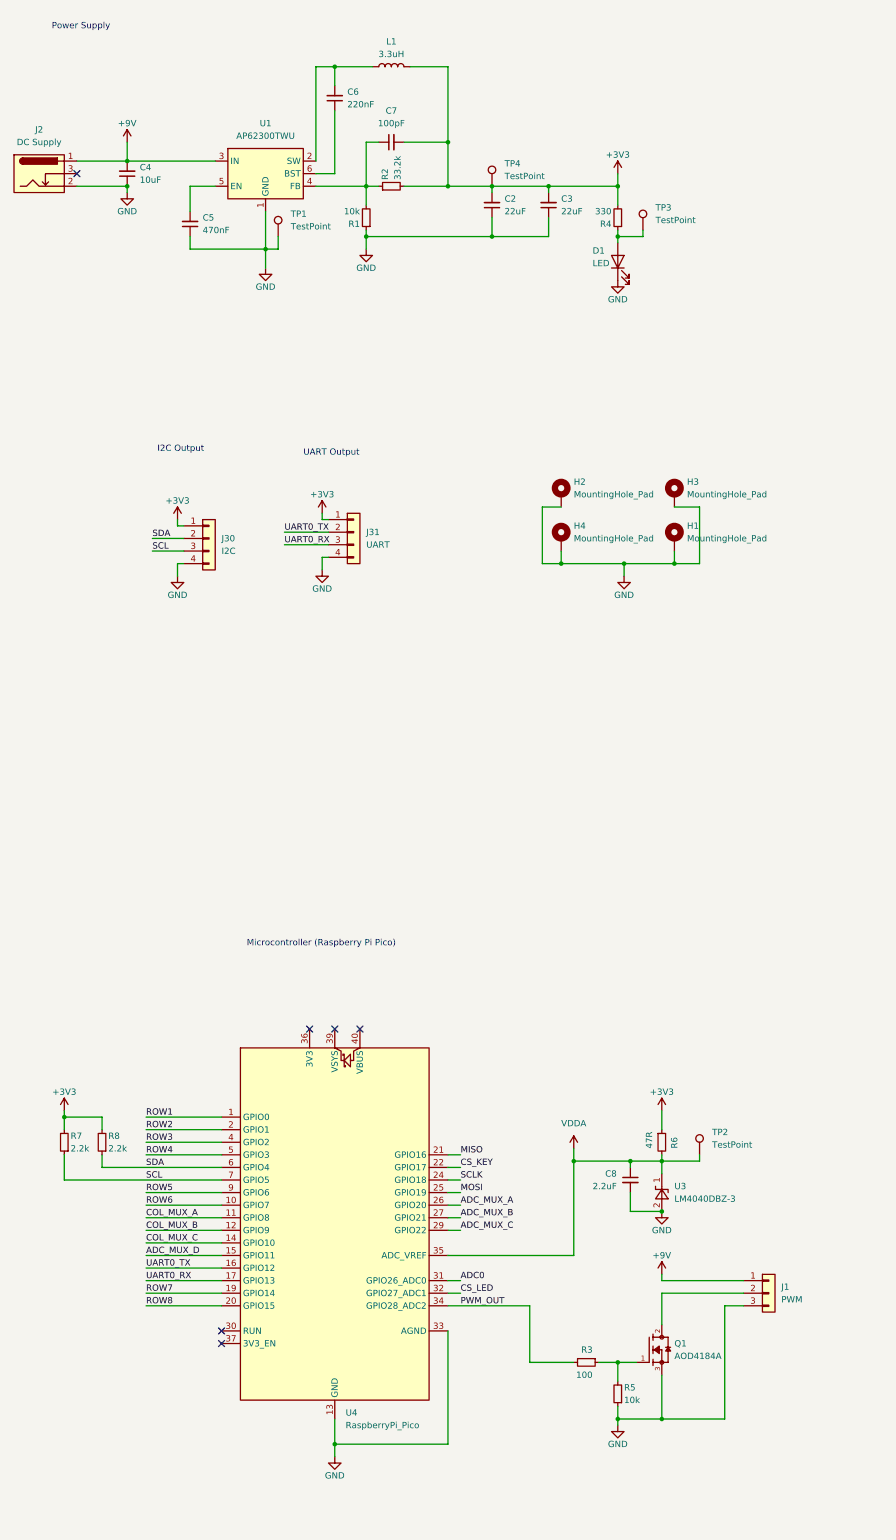
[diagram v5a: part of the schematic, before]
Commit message: Improving PWM circuit
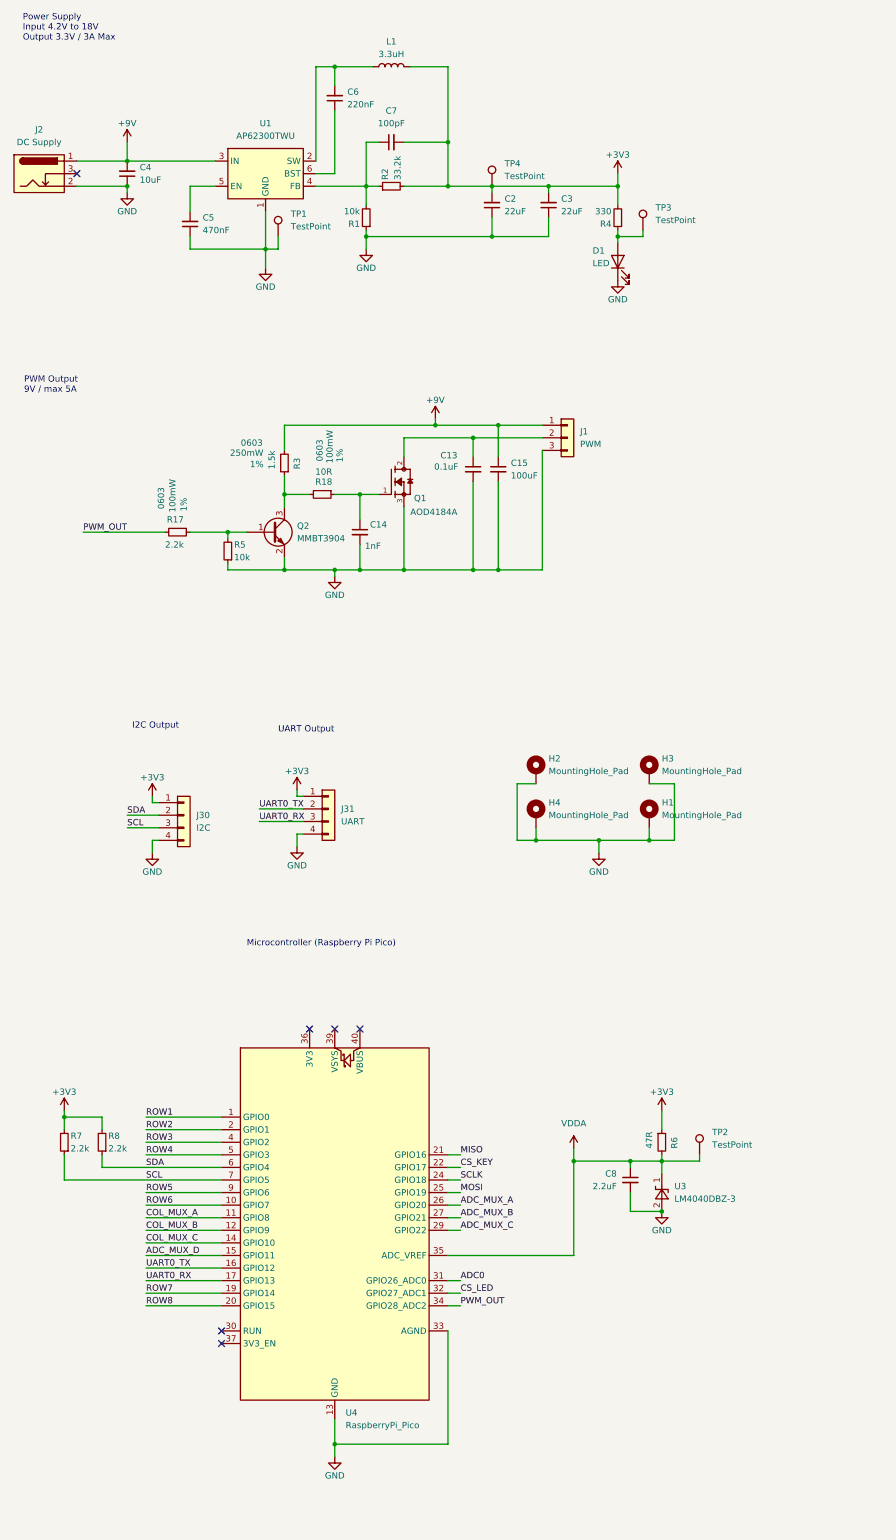
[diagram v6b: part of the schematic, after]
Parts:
- added C13: 0.1uF, Capacitor_SMD:C_0201_0603Metric_Pad0.64x0.40mm_HandSolder, symbol Device:C_Small
- added C14: 1nF, Capacitor_SMD:C_0201_0603Metric_Pad0.64x0.40mm_HandSolder, symbol Device:C_Small
- added C15: 100uF, Capacitor_SMD:C_0201_0603Metric_Pad0.64x0.40mm_HandSolder, symbol Device:C_Small
- added Q2: MMBT3904, Package_TO_SOT_SMD:SOT-23, symbol Transistor_BJT:MMBT3904
- added R17: 2.2k, Resistor_SMD:R_0603_1608Metric_Pad0.98x0.95mm_HandSolder, symbol Device:R_Small
- added R18: 10R, Resistor_SMD:R_0603_1608Metric_Pad0.98x0.95mm_HandSolder, symbol Device:R_Small
- R3: value 100 -> 1.5k; JLCPCB Part # C22775 -> C543357; Power 100mW -> 250mW
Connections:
- net +9V: now also R3.2, C15.1
- net GND: now also C13.2, C14.2, C15.2, Q2.2 (E)
- net PWM_OUT: now also R17.2; no longer R3.2
- net at J1.2 (Pin_2), Q1.2: now also C13.1
- new net: C14.1, Q1.1, R18.1
- new net: Q2.1 (B), R17.1, R5.2
- new net: Q2.3 (C), R18.2, R3.1
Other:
- note added: "PWM Output 9V / max 5A"
- note added: "Power Supply Input 4.2V to 18V Output 3.3V / 3A Max"
- note removed: "Power Supply"
- moved on the sheet: H1, H2, H3, H4, J1, J30, J31, Q1, R3, R5
